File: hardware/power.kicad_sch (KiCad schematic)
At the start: 87 parts, among them J3 Vcore_sel, U1 TLV62569DBV, U2 TLV62569DBV, U3 MPM3833CGRH-Z, U4 GateMate-CCGM1A1, U5 TLV62569DBV

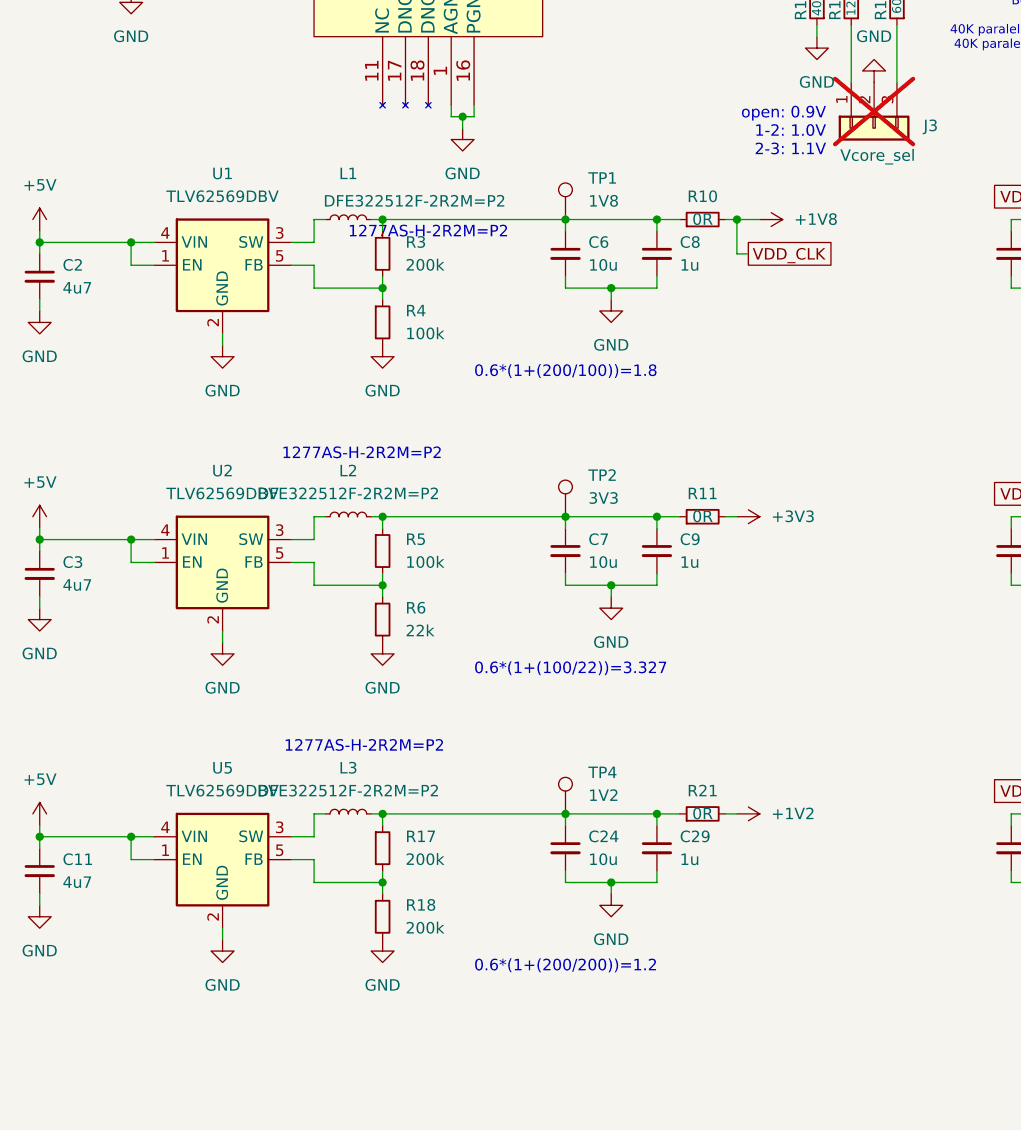
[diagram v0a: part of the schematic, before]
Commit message: power: change gpio dc converter to ldo
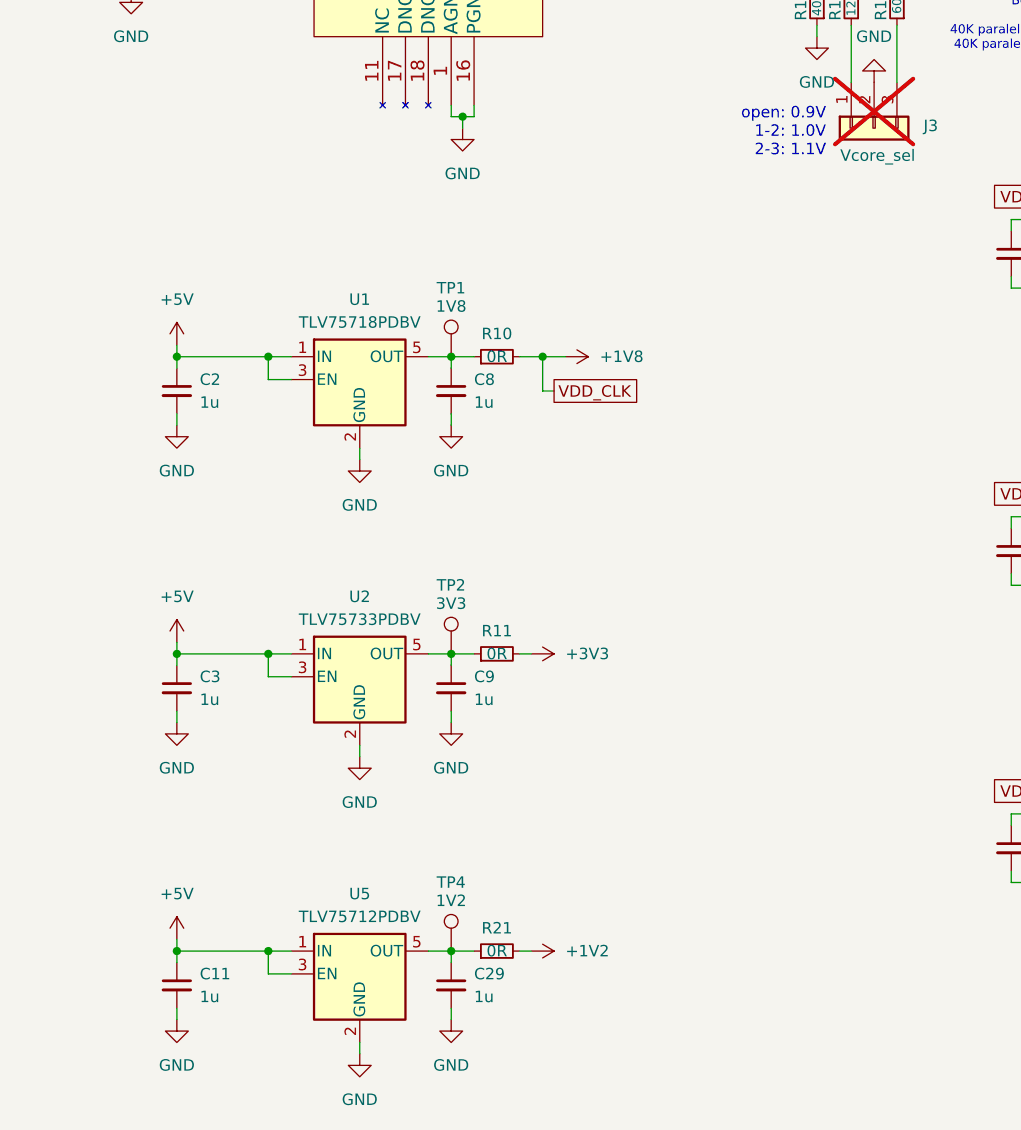
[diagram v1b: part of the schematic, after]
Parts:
- removed C24, C6, C7: 10u, Capacitor_SMD:C_0402_1005Metric, symbol Device:C_Small
- removed L1, L2, L3: DFE322512F-2R2M=P2, Inductor_SMD:L_1008_2520Metric, symbol Device:L_Small
- removed R17, R18, R3: 200k, Resistor_SMD:R_0402_1005Metric, symbol Device:R_Small
- removed R4, R5: 100k, Resistor_SMD:R_0402_1005Metric, symbol Device:R_Small
- removed R6: 22k, Resistor_SMD:R_0402_1005Metric, symbol Device:R_Small
- removed U1, U2, U5: TLV62569DBV, Package_TO_SOT_SMD:SOT-23-5, symbol Regulator_Switching:TLV62569DBV
- added U1: TLV75718PDBV, Package_TO_SOT_SMD:SOT-23-5, symbol Regulator_Linear:TLV75718PDBV
- added U2: TLV75733PDBV, Package_TO_SOT_SMD:SOT-23-5, symbol Regulator_Linear:TLV75733PDBV
- added U5: TLV75712PDBV, Package_TO_SOT_SMD:SOT-23-5, symbol Regulator_Linear:TLV75712PDBV
- C11, C2, C3: value 4u7 -> 1u; footprint Capacitor_SMD:C_0402_1005Metric -> Capacitor_SMD:C_0603_1608Metric
- C29, C8, C9: footprint Capacitor_SMD:C_0402_1005Metric -> Capacitor_SMD:C_0603_1608Metric
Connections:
- net +5V: now also U1.1 (IN), U1.3 (EN), U2.1 (IN), U2.3 (EN), U5.1 (IN), U5.3 (EN)
- net GND: now also U1.2 (GND), U2.2 (GND), U5.2 (GND)
- net at C9.1, R11.1, TP2.1: now also U2.5 (OUT)
- net at C8.1, R10.1, TP1.1: now also U1.5 (OUT)
- net at C29.1, R21.1, TP4.1: now also U5.5 (OUT)
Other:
- note removed: "0.6*(1+(100/22))=3.327"
- note removed: "0.6*(1+(200/100))=1.8"
- note removed: "0.6*(1+(200/200))=1.2"
- note removed: "1277AS-H-2R2M=P2"
- moved on the sheet: C11, C2, C29, C3, C8, C9, R10, R11, R21, TP1

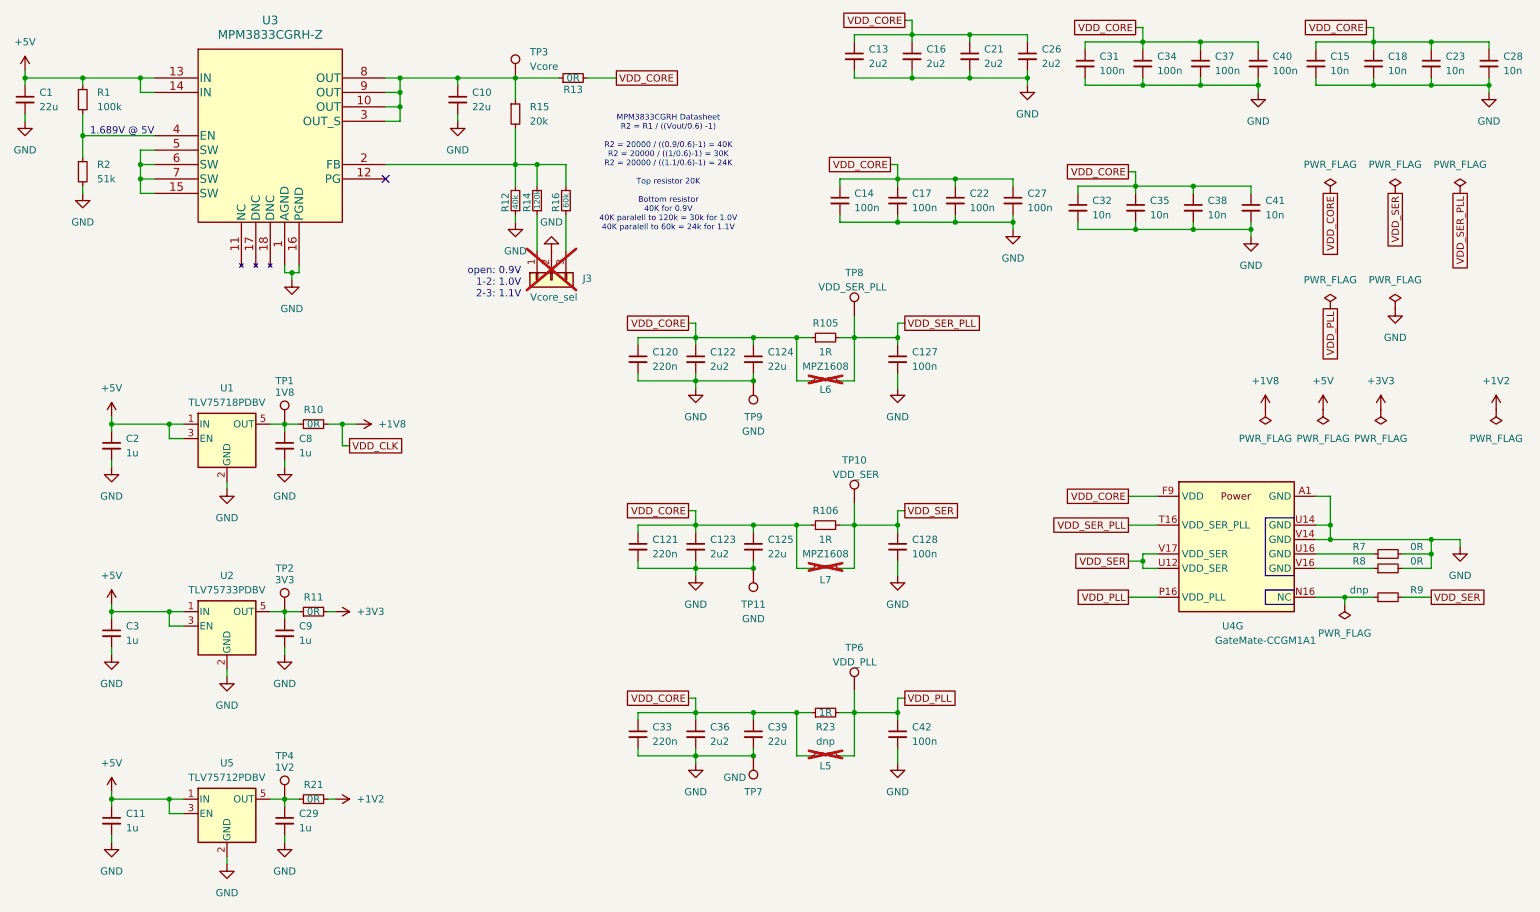
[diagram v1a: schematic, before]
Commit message: power: reduce decoupling capacitors
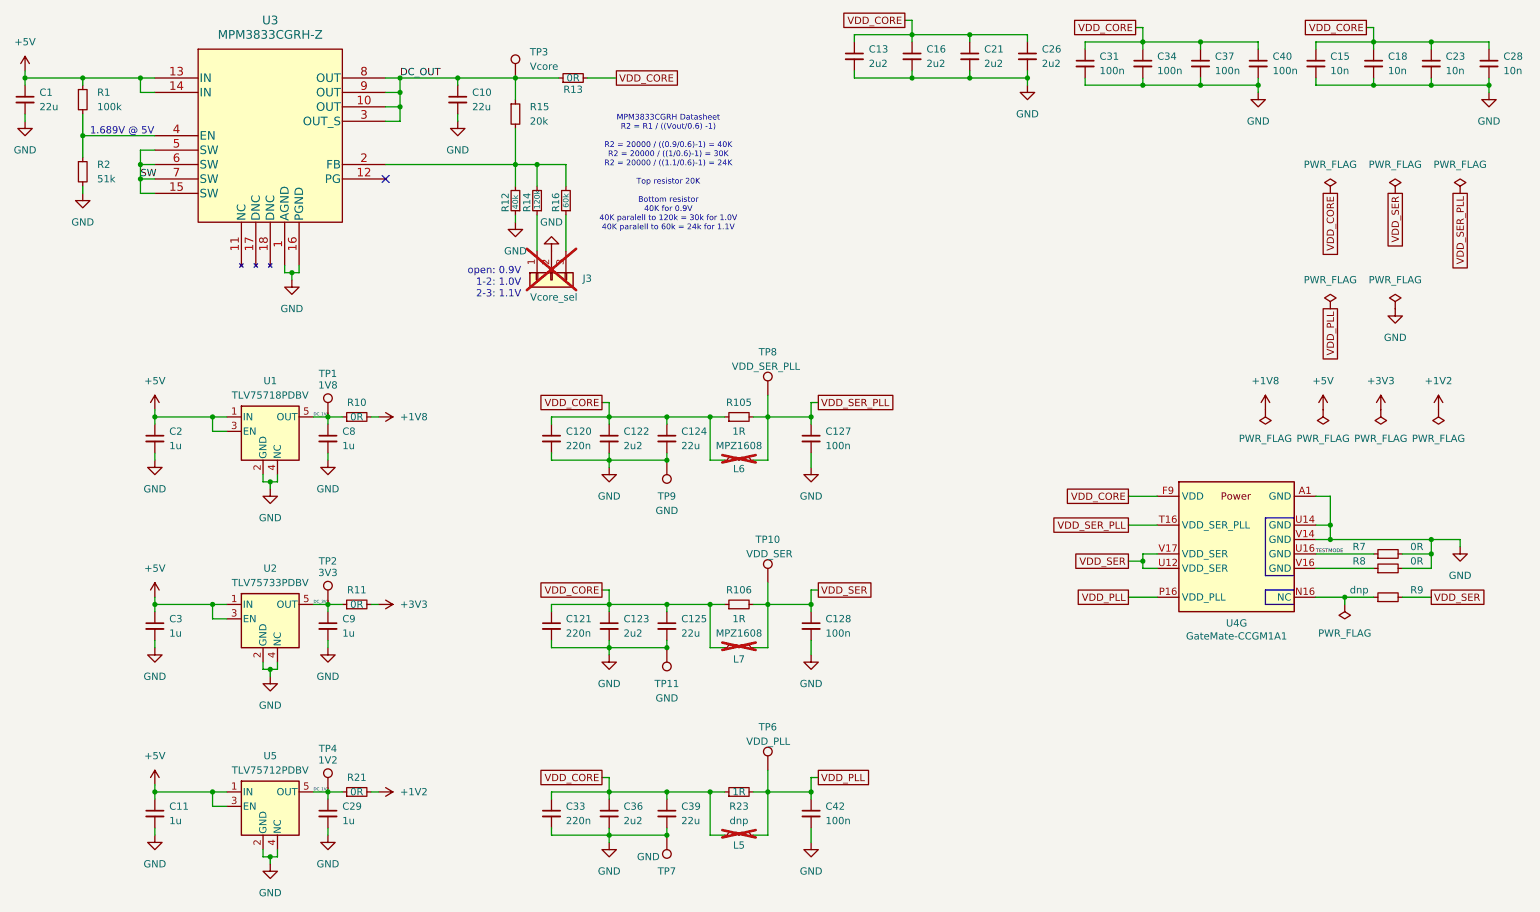
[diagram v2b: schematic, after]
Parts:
- removed C14, C17, C22, C27: 100n, Capacitor_SMD:C_0402_1005Metric, symbol Device:C_Small
- removed C32, C35, C38, C41: 10n, Capacitor_SMD:C_0402_1005Metric, symbol Device:C_Small
- R10, R11, R13, R21: footprint Resistor_SMD:R_0603_1608Metric -> Resistor_SMD:R_0805_2012Metric
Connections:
- net GND: now also U1.4 (NC), U2.4 (NC), U5.4 (NC)
- net DC_3V3: now reaches C9.1, R11.1, TP2.1, U2.5 (OUT)
- net DC_1V8: now reaches C8.1, R10.1, TP1.1, U1.5 (OUT)
- net DC_1V2: now reaches C29.1, R21.1, TP4.1, U5.5 (OUT)
- net DC_OUT: now reaches C10.1, R13.1, R15.1, TP3.1, U3.10 (OUT), U3.3 (OUT_S), U3.8 (OUT), U3.9 (OUT)
- net TESTMODE: now reaches R7.1, U4.U16 (GND)
- net SW: now reaches U3.15 (SW), U3.5 (SW), U3.6 (SW), U3.7 (SW)
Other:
- moved on the sheet: C11, C120, C121, C122, C123, C124, C125, C127, C128, C2, C29, C3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
